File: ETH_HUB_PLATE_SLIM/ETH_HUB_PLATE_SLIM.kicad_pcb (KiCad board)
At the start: 2 copper layers, 60.5 x 54.4 mm, 6 parts

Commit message: minor adjustments to holes
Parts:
- moved REF** 0.46 mm to (156.2, 141.1)
- moved REF** 0.35 mm to (156.2, 104.0)
- moved REF** 0.30 mm to (104.0, 141.1)
- moved REF** 0.20 mm to (123.0, 105.4)
- moved REF** 0.10 mm to (129.9, 133.7)
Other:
- board size 60.5 x 54.4 mm -> 60.2 x 54.4 mm
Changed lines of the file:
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@@
   )
   (module MountingHole:MountingHole_3.2mm_M3 (layer F.Cu)
-    (at 130 133.7)
+    (at 129.9 133.7)
     (descr "Mounting Hole 3.2mm, no annular, M3")
     (tags "mounting hole 3.2mm no annular m3")
@@
   )
   (module MountingHole:MountingHole_3.2mm_M3 (layer F.Cu)
-    (at 122.8 105.4)
+    (at 123 105.4)
     (descr "Mounting Hole 3.2mm, no annular, M3")
     (tags "mounting hole 3.2mm no annular m3")
@@
   )
   (module MountingHole:MountingHole_3.2mm_M3 (layer F.Cu)
-    (at 156.5 141.4)
+    (at 156.15 141.1)
     (descr "Mounting Hole 3.2mm, no annular, M3")
     (tags "mounting hole 3.2mm no annular m3")
@@
   )
   (module MountingHole:MountingHole_3.2mm_M3 (layer F.Cu)
-    (at 104 141.4)
+    (at 104 141.1)
     (descr "Mounting Hole 3.2mm, no annular, M3")
     (tags "mounting hole 3.2mm no annular m3")
@@
   )
   (module MountingHole:MountingHole_3.2mm_M3 (layer F.Cu)
-    (at 156.5 104)
+    (at 156.15 104)
     (descr "Mounting Hole 3.2mm, no annular, M3")
     (tags "mounting hole 3.2mm no annular m3")
@@
     (pad 1 np_thru_hole circle (at 0 0) (size 3.2 3.2) (drill 3.2) (layers *.Cu *.Mask))
   )
-  (gr_line (start 100 145.4) (end 160.5 145.4) (layer F.SilkS) (width 0.12))
-  (gr_line (start 100 154.4) (end 160.5 154.4) (layer Edge.Cuts) (width 0.05))
-  (gr_line (start 160.5 100) (end 160.5 154.4) (layer Edge.Cuts) (width 0.05))
-  (gr_line (start 100 100) (end 160.5 100) (layer Edge.Cuts) (width 0.05))
+  (gr_line (start 100 145.4) (end 160.15 145.4) (layer F.SilkS) (width 0.12))
+  (gr_line (start 100 154.4) (end 160.15 154.4) (layer Edge.Cuts) (width 0.05))
+  (gr_line (start 160.15 100) (end 160.15 154.4) (layer Edge.Cuts) (width 0.05))
+  (gr_line (start 100 100) (end 160.15 100) (layer Edge.Cuts) (width 0.05))
   (gr_line (start 100 100) (end 100 154.4) (layer Edge.Cuts) (width 0.05))
 )

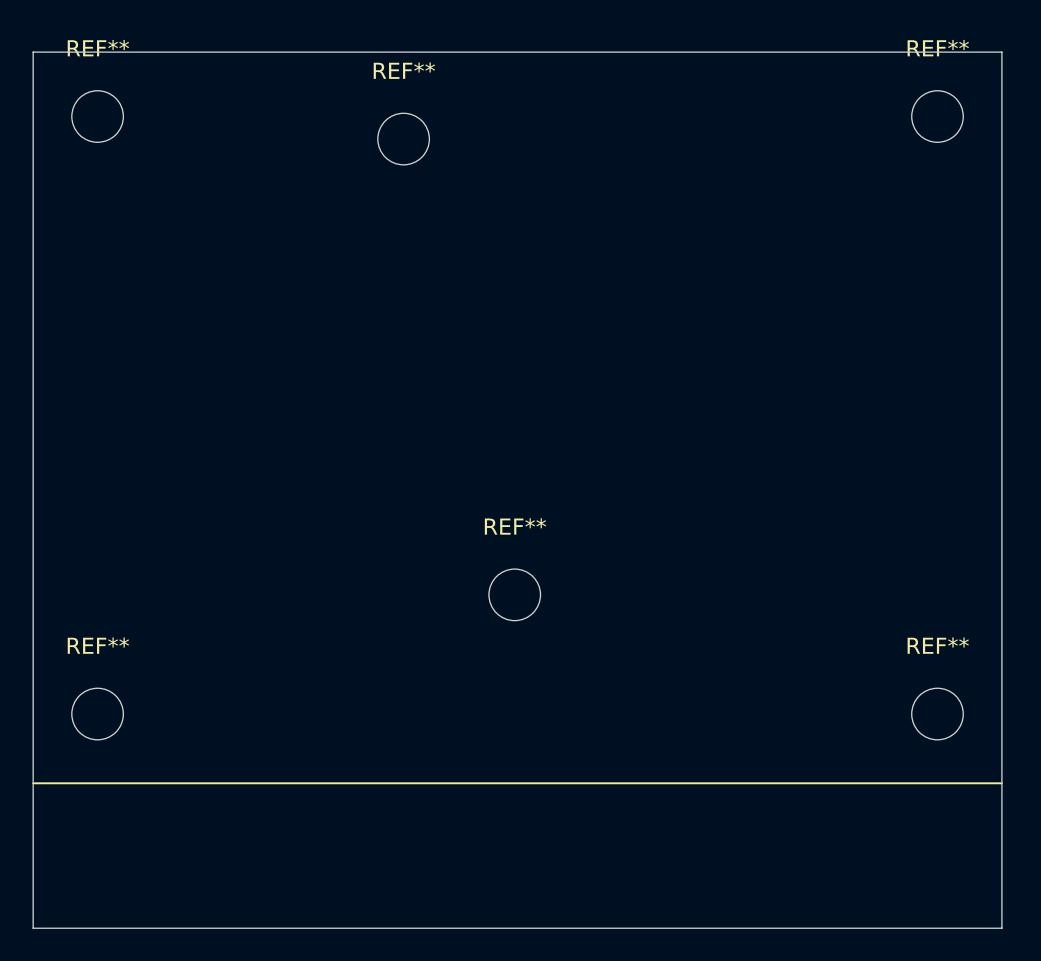
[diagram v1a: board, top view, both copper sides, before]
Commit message: copper plates and silks
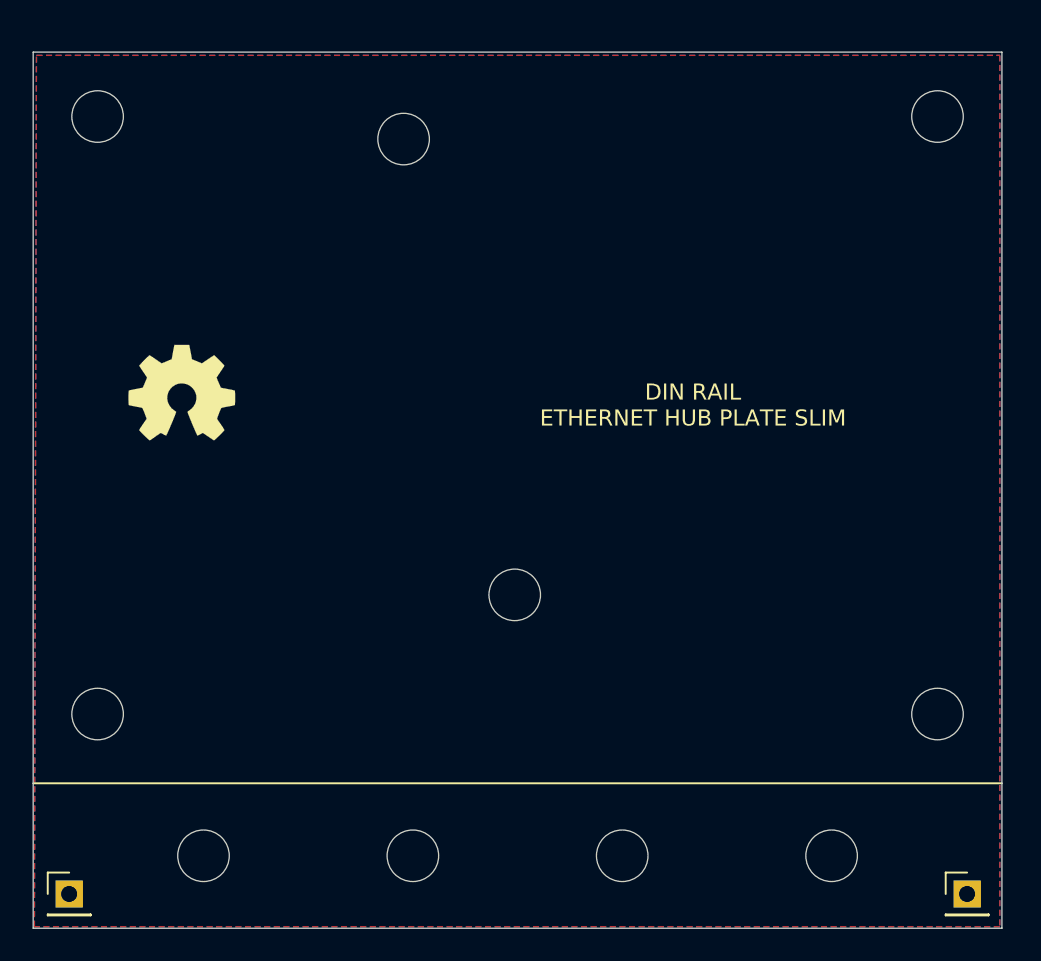
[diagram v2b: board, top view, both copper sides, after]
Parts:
- added J1: Conn_01x01_Male, Connector_PinHeader_2.54mm:PinHeader_1x01_P2.54mm_Vertical, F.Cu at (102.2, 152.3)
- added J2: Conn_01x01_Male, Connector_PinHeader_2.54mm:PinHeader_1x01_P2.54mm_Vertical, F.Cu at (158.0, 152.3)
- added REF**: OSHW-Symbol_6.7x6mm_SilkScreen, Symbol:OSHW-Symbol_6.7x6mm_SilkScreen, B.Cu at (150.0, 120.9)
- added REF**: OSHW-Symbol_6.7x6mm_SilkScreen, Symbol:OSHW-Symbol_6.7x6mm_SilkScreen, F.Cu at (109.2, 121.2)
- added REF**: MountingHole_3.2mm_M3, MountingHole:MountingHole_3.2mm_M3, F.Cu at (110.6, 149.9)
- added REF**: MountingHole_3.2mm_M3, MountingHole:MountingHole_3.2mm_M3, F.Cu at (149.6, 149.9)
- added REF**: MountingHole_3.2mm_M3, MountingHole:MountingHole_3.2mm_M3, F.Cu at (136.6, 149.9)
- added REF**: MountingHole_3.2mm_M3, MountingHole:MountingHole_3.2mm_M3, F.Cu at (123.6, 149.9)
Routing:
- added copper zone on B.Cu, net Net-(J1-Pad1)
- added copper zone on F.Cu, net Net-(J1-Pad1)
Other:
- board text added: "DIN RAIL ETHERNET HUB PLATE SLIM"
